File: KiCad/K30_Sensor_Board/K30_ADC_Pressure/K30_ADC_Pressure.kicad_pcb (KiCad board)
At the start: 2 copper layers, 100 x 50.8 mm, 156 parts, among them J1 CONN_02X12, J2 CONN_01X03, J3 CONN_01X05, J4 CONN_01X03, U1 ADS1015_VSSOP, U2 LPS25HB_HLGA

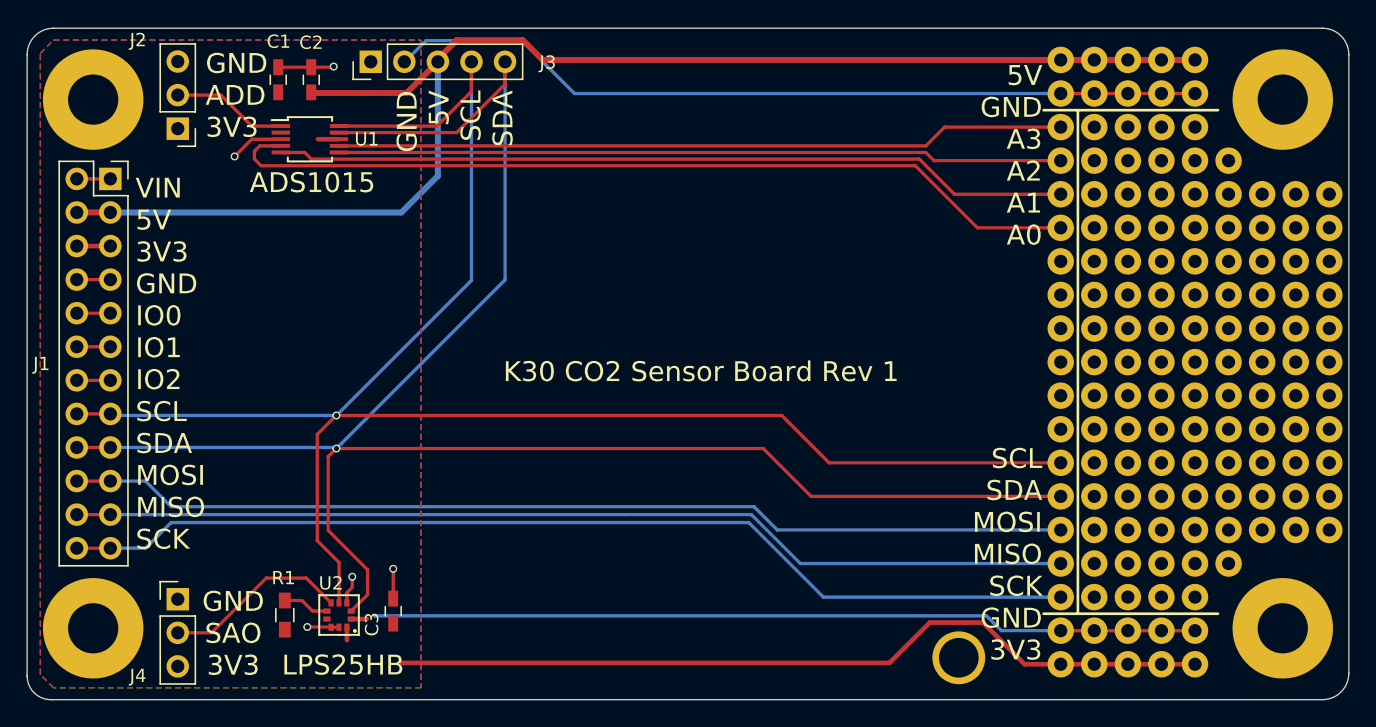
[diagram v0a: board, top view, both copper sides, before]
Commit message: minor changes to mounting hole
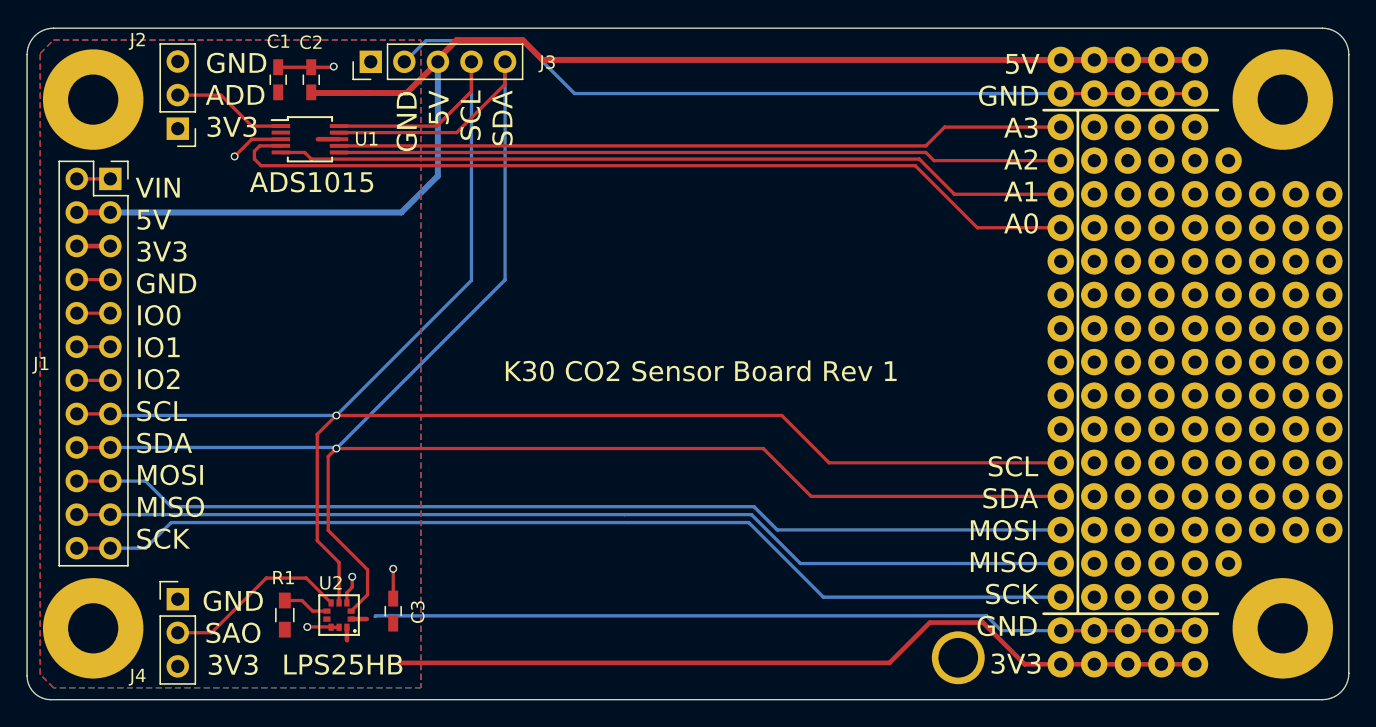
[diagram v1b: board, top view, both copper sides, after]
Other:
- rule trace_min: 0.2 -> 0.152
- board text added: "3V3"
- board text added: "5V GND A3 A2 A1 A0"
- board text added: "SCL SDA MOSI MISO SCK GND"
- board text removed: "5V GND A3 A2 A1 A0 SCL SDA MOSI MISO SCK GND 3V3"
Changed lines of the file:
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@@
     (area 90.745714 72.766666 204.069287 127.51)
     (thickness 1.6)
-    (drawings 20)
+    (drawings 22)
     (tracks 160)
     (zones 0)
@@
     (zone_clearance 0.508)
     (zone_45_only no)
-    (trace_min 0.2)
+    (trace_min 0.152)
     (segment_width 0.2)
     (edge_width 0.1)
@@
     (visible_elements 7FFCFFFF)
     (pcbplotparams
-      (layerselection 0x00030_80000001)
+      (layerselection 0x010f0_80000001)
       (usegerberextensions false)
       (excludeedgelayer true)
@@
       (outputformat 1)
       (mirror false)
-      (drillshape 1)
+      (drillshape 0)
       (scaleselection 1)
       (outputdirectory ""))
@@
   )
   (module Wire_Pads:SolderWirePad_single_1mmDrill (layer F.Cu)
-    (at 166.09 122.83)
+    (at 166.05 122.83)
     (fp_text reference REF** (at 0 -3.81) (layer F.SilkS) hide
       (effects (font (size 1 1) (thickness 0.15)))
@@
     (tags "capacitor 0603")
     (attr smd)
-    (fp_text reference C3 (at -1 -1.6 270) (layer F.SilkS)
+    (fp_text reference C3 (at -0.06 1.89 90) (layer F.SilkS)
       (effects (font (size 1 1) (thickness 0.15)))
     )
@@
       (net 2 /5V))
   )
+  (gr_text 3V3 (at 170.43 123.33) (layer F.SilkS)
+    (effects (font (size 1.5 1.5) (thickness 0.3)))
+  )
+  (gr_text "SCL\nSDA\nMOSI\nMISO\nSCK\nGND" (at 172.11 114.44) (layer F.SilkS)
+    (effects (font (size 1.5 1.5) (thickness 0.3)) (justify right))
+  )
   (gr_line (start 166.09 122.82) (end 166.09 122.83) (angle 90) (layer Eco1.User) (width 0.2))
   (gr_text "GND\nADD\n3V3" (at 109.1 80.3) (layer F.SilkS)
@@
     (effects (font (size 1.5 1.5) (thickness 0.3)))
   )
-  (gr_text "5V\nGND\nA3\nA2\nA1\nA0\n\n\n\n\n\n\nSCL\nSDA\nMOSI\nMISO\nSCK\nGND\n3V3" (at 172.42 100.53) (layer F.SilkS)
+  (gr_text "5V\nGND\nA3\nA2\nA1\nA0" (at 172.22 83.99) (layer F.SilkS)
     (effects (font (size 1.5 1.5) (thickness 0.3)) (justify right))
   )
@@
   (segment (start 133.1 76.1) (end 134.6 77.6) (width 0.45) (layer F.Cu) (net 2))
   (segment (start 128.1 76.1) (end 133.1 76.1) (width 0.45) (layer F.Cu) (net 2))
-  (segment (start 124.14 77.74) (end 124.18 77.74) (width 0.25) (layer B.Cu) (net 3) (status C00000))
-  (segment (start 124.18 77.74) (end 125.78 76.14) (width 0.25) (layer B.Cu) (net 3) (status 400000))
-  (segment (start 137.02 80.14) (end 173.8 80.14) (width 0.25) (layer B.Cu) (net 3) (status 800000))
+  (segment (start 124.14 77.74) (end 124.18 77.74) (width 0.25) (layer B.Cu) (net 3))
+  (segment (start 124.18 77.74) (end 125.78 76.14) (width 0.25) (layer B.Cu) (net 3))
+  (segment (start 137.02 80.14) (end 173.8 80.14) (width 0.25) (layer B.Cu) (net 3))
   (segment (start 133.02 76.14) (end 137.02 80.14) (width 0.25) (layer B.Cu) (net 3))
   (segment (start 125.78 76.14) (end 133.02 76.14) (width 0.25) (layer B.Cu) (net 3))
@@
   (segment (start 99.36 101.84) (end 101.9 101.84) (width 0.25) (layer F.Cu) (net 7))
   (segment (start 119 107) (end 118.98 107) (width 0.25) (layer F.Cu) (net 8))
-  (segment (start 121.36 118.06) (end 120.12 119.3) (width 0.25) (layer F.Cu) (net 8) (status 800000))
+  (segment (start 121.36 118.06) (end 120.12 119.3) (width 0.25) (layer F.Cu) (net 8))
   (segment (start 121.36 116.17) (end 121.36 118.06) (width 0.25) (layer F.Cu) (net 8))
   (segment (start 118.38 113.19) (end 121.36 116.17) (width 0.25) (layer F.Cu) (net 8))
@@
   (segment (start 101.9 106.92) (end 101.9 106.9) (width 0.25) (layer B.Cu) (net 8))
   (segment (start 119 104.5) (end 118.98 104.5) (width 0.25) (layer F.Cu) (net 9))
-  (segment (start 119.2 115.62) (end 119.2 118.68) (width 0.25) (layer F.Cu) (net 9) (status 800000))
+  (segment (start 119.2 115.62) (end 119.2 118.68) (width 0.25) (layer F.Cu) (net 9))
   (segment (start 117.55 113.97) (end 119.2 115.62) (width 0.25) (layer F.Cu) (net 9))
   (segment (start 117.55 105.93) (end 117.55 113.97) (width 0.25) (layer F.Cu) (net 9))

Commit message: added other kicad projects, sketchup solar model
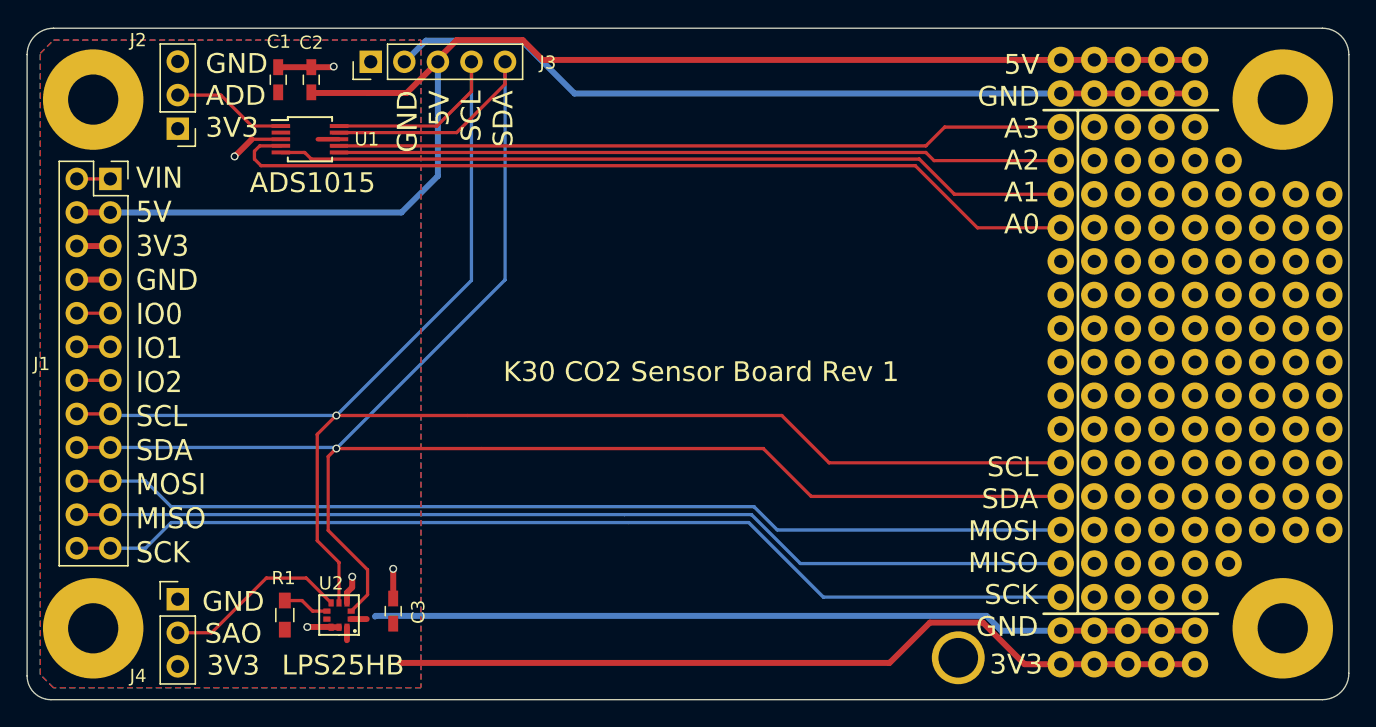
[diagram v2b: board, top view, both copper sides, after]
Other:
- net class 3V3: trace_width 0.35 -> 0.45
- net class GND added: clearance 0.14, trace_width 0.45, via_dia 0.6, via_drill 0.4
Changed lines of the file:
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@@
     (add_net /SDA)
     (add_net /VIN)
-    (add_net GND)
     (add_net "Net-(J2-Pad2)")
     (add_net "Net-(J3-Pad1)")
@@
   (net_class 3V3 ""
     (clearance 0.14)
-    (trace_width 0.35)
+    (trace_width 0.45)
     (via_dia 0.6)
     (via_drill 0.4)
@@
     (uvia_drill 0.1)
     (add_net /5V)
+  )
+  (net_class GND ""
+    (clearance 0.14)
+    (trace_width 0.45)
+    (via_dia 0.6)
+    (via_drill 0.4)
+    (uvia_dia 0.3)
+    (uvia_drill 0.1)
+    (add_net GND)
   )
   (module Wire_Pads:SolderWirePad_single_1mmDrill (layer F.Cu)
@@
     (effects (font (size 1.5 1.5) (thickness 0.3)))
   )
-  (gr_text "VIN\n5V\n3V3\nGND\nIO0\nIO1\nIO2\nSCL\nSDA\nMOSI\nMISO\nSCK" (at 103.8 100.6) (layer F.SilkS)
-    (effects (font (size 1.5 1.5) (thickness 0.3)) (justify left))
-  )
-  (segment (start 173.8 123.32) (end 171.07 123.32) (width 0.35) (layer F.Cu) (net 1))
-  (segment (start 123.87 123.22) (end 123.83 123.18) (width 0.35) (layer F.Cu) (net 1))
-  (segment (start 160.85 123.22) (end 123.87 123.22) (width 0.35) (layer F.Cu) (net 1))
-  (segment (start 163.9 120.17) (end 160.85 123.22) (width 0.35) (layer F.Cu) (net 1))
-  (segment (start 167.92 120.17) (end 163.9 120.17) (width 0.35) (layer F.Cu) (net 1))
-  (segment (start 171.07 123.32) (end 167.92 120.17) (width 0.35) (layer F.Cu) (net 1))
+  (gr_text "VIN\n5V\n3V3\nGND\nIO0\nIO1\nIO2\nSCL\nSDA\nMOSI\nMISO\nSCK" (at 103.83 100.7) (layer F.SilkS)
+    (effects (font (size 1.6 1.5) (thickness 0.3)) (justify left))
+  )
+  (segment (start 173.8 123.32) (end 171.07 123.32) (width 0.45) (layer F.Cu) (net 1))
+  (segment (start 123.87 123.22) (end 123.83 123.18) (width 0.45) (layer F.Cu) (net 1))
+  (segment (start 160.85 123.22) (end 123.87 123.22) (width 0.45) (layer F.Cu) (net 1))
+  (segment (start 163.9 120.17) (end 160.85 123.22) (width 0.45) (layer F.Cu) (net 1))
+  (segment (start 167.92 120.17) (end 163.9 120.17) (width 0.45) (layer F.Cu) (net 1))
+  (segment (start 171.07 123.32) (end 167.92 120.17) (width 0.45) (layer F.Cu) (net 1))
   (segment (start 119.2 83.6) (end 117.6 83.6) (width 0.35) (layer F.Cu) (net 1))
-  (segment (start 119.8 120.52) (end 119.8 121.5) (width 0.35) (layer F.Cu) (net 1))
-  (segment (start 120.12 119.9) (end 121.3 119.9) (width 0.35) (layer F.Cu) (net 1))
-  (segment (start 183.96 123.32) (end 181.42 123.32) (width 0.35) (layer F.Cu) (net 1))
-  (segment (start 181.42 123.32) (end 178.88 123.32) (width 0.35) (layer F.Cu) (net 1))
-  (segment (start 178.88 123.32) (end 176.34 123.32) (width 0.35) (layer F.Cu) (net 1))
-  (segment (start 176.34 123.32) (end 173.8 123.32) (width 0.35) (layer F.Cu) (net 1))
-  (segment (start 99.36 91.68) (end 101.9 91.68) (width 0.35) (layer F.Cu) (net 1))
+  (segment (start 119.8 120.52) (end 119.8 121.5) (width 0.45) (layer F.Cu) (net 1))
+  (segment (start 120.12 119.9) (end 121.3 119.9) (width 0.45) (layer F.Cu) (net 1))
+  (segment (start 183.96 123.32) (end 181.42 123.32) (width 0.45) (layer F.Cu) (net 1))
+  (segment (start 181.42 123.32) (end 178.88 123.32) (width 0.45) (layer F.Cu) (net 1))
+  (segment (start 178.88 123.32) (end 176.34 123.32) (width 0.45) (layer F.Cu) (net 1))
+  (segment (start 176.34 123.32) (end 173.8 123.32) (width 0.45) (layer F.Cu) (net 1))
+  (segment (start 99.36 91.68) (end 101.9 91.68) (width 0.45) (layer F.Cu) (net 1))
   (segment (start 126.68 77.74) (end 126.68 86.38) (width 0.45) (layer B.Cu) (net 2))
   (segment (start 123.92 89.14) (end 101.9 89.14) (width 0.45) (layer B.Cu) (net 2))
@@
   (segment (start 133.1 76.1) (end 134.6 77.6) (width 0.45) (layer F.Cu) (net 2))
   (segment (start 128.1 76.1) (end 133.1 76.1) (width 0.45) (layer F.Cu) (net 2))
-  (segment (start 124.14 77.74) (end 124.18 77.74) (width 0.25) (layer B.Cu) (net 3))
-  (segment (start 124.18 77.74) (end 125.78 76.14) (width 0.25) (layer B.Cu) (net 3))
-  (segment (start 137.02 80.14) (end 173.8 80.14) (width 0.25) (layer B.Cu) (net 3))
-  (segment (start 133.02 76.14) (end 137.02 80.14) (width 0.25) (layer B.Cu) (net 3))
-  (segment (start 125.78 76.14) (end 133.02 76.14) (width 0.25) (layer B.Cu) (net 3))
-  (segment (start 173.8 120.78) (end 169.31 120.78) (width 0.25) (layer B.Cu) (net 3))
-  (segment (start 121.97 119.66) (end 121.92 119.71) (width 0.25) (layer B.Cu) (net 3))
-  (segment (start 168.19 119.66) (end 121.97 119.66) (width 0.25) (layer B.Cu) (net 3))
-  (segment (start 169.31 120.78) (end 168.19 119.66) (width 0.25) (layer B.Cu) (net 3))
+  (segment (start 124.14 77.74) (end 124.18 77.74) (width 0.45) (layer B.Cu) (net 3))
+  (segment (start 124.18 77.74) (end 125.78 76.14) (width 0.45) (layer B.Cu) (net 3))
+  (segment (start 137.02 80.14) (end 173.8 80.14) (width 0.45) (layer B.Cu) (net 3))
+  (segment (start 133.02 76.14) (end 137.02 80.14) (width 0.45) (layer B.Cu) (net 3))
+  (segment (start 125.78 76.14) (end 133.02 76.14) (width 0.45) (layer B.Cu) (net 3))
+  (segment (start 173.8 120.78) (end 169.31 120.78) (width 0.45) (layer B.Cu) (net 3))
+  (segment (start 121.97 119.66) (end 121.92 119.71) (width 0.45) (layer B.Cu) (net 3))
+  (segment (start 168.19 119.66) (end 121.97 119.66) (width 0.45) (layer B.Cu) (net 3))
+  (segment (start 169.31 120.78) (end 168.19 119.66) (width 0.45) (layer B.Cu) (net 3))
   (segment (start 114.8 83.6) (end 112.6 83.6) (width 0.25) (layer F.Cu) (net 3))
   (via (at 111.3 84.9) (size 0.6) (drill 0.4) (layers F.Cu B.Cu) (net 3))
-  (segment (start 112.6 83.6) (end 111.3 84.9) (width 0.25) (layer F.Cu) (net 3))
-  (segment (start 114.6 78.15) (end 117.1 78.15) (width 0.25) (layer F.Cu) (net 3))
-  (segment (start 119.8 118.68) (end 119.8 117.9) (width 0.25) (layer F.Cu) (net 3))
+  (segment (start 112.6 83.6) (end 111.3 84.9) (width 0.45) (layer F.Cu) (net 3))
+  (segment (start 114.6 78.15) (end 117.1 78.15) (width 0.45) (layer F.Cu) (net 3))
+  (segment (start 119.8 118.68) (end 119.8 117.9) (width 0.45) (layer F.Cu) (net 3))
   (via (at 120.2 116.7) (size 0.6) (drill 0.4) (layers F.Cu B.Cu) (net 3))
-  (segment (start 120.2 117.5) (end 120.2 116.7) (width 0.25) (layer F.Cu) (net 3))
-  (segment (start 119.8 117.9) (end 120.2 117.5) (width 0.25) (layer F.Cu) (net 3))
-  (segment (start 123.3 118.35) (end 123.3 116.1) (width 0.25) (layer F.Cu) (net 3))
+  (segment (start 120.2 117.5) (end 120.2 116.7) (width 0.45) (layer F.Cu) (net 3))
+  (segment (start 119.8 117.9) (end 120.2 117.5) (width 0.45) (layer F.Cu) (net 3))
+  (segment (start 123.3 118.35) (end 123.3 116.1) (width 0.45) (layer F.Cu) (net 3))
   (via (at 123.3 116.1) (size 0.6) (drill 0.4) (layers F.Cu B.Cu) (net 3))
-  (segment (start 119.2 120.52) (end 118.6 120.52) (width 0.25) (layer F.Cu) (net 3))
-  (segment (start 118.6 120.52) (end 118.58 120.5) (width 0.25) (layer F.Cu) (net 3))
-  (segment (start 118.58 120.5) (end 116.8 120.5) (width 0.25) (layer F.Cu) (net 3))
+  (segment (start 119.2 120.52) (end 118.6 120.52) (width 0.45) (layer F.Cu) (net 3))
+  (segment (start 118.6 120.52) (end 118.58 120.5) (width 0.45) (layer F.Cu) (net 3))
+  (segment (start 118.58 120.5) (end 116.8 120.5) (width 0.45) (layer F.Cu) (net 3))
   (via (at 116.8 120.5) (size 0.6) (drill 0.4) (layers F.Cu B.Cu) (net 3))
-  (segment (start 173.8 120.78) (end 176.34 120.78) (width 0.25) (layer F.Cu) (net 3))
-  (segment (start 176.34 120.78) (end 178.88 120.78) (width 0.25) (layer F.Cu) (net 3))
-  (segment (start 178.88 120.78) (end 181.42 120.78) (width 0.25) (layer F.Cu) (net 3))
-  (segment (start 181.42 120.78) (end 183.96 120.78) (width 0.25) (layer F.Cu) (net 3))
-  (segment (start 173.8 80.14) (end 176.34 80.14) (width 0.25) (layer F.Cu) (net 3))
-  (segment (start 176.34 80.14) (end 178.88 80.14) (width 0.25) (layer F.Cu) (net 3))
-  (segment (start 178.88 80.14) (end 181.42 80.14) (width 0.25) (layer F.Cu) (net 3))
-  (segment (start 181.42 80.14) (end 183.96 80.14) (width 0.25) (layer F.Cu) (net 3))
-  (segment (start 99.36 94.22) (end 101.9 94.22) (width 0.25) (layer F.Cu) (net 3))
-  (segment (start 117.1 78.15) (end 118.75 78.15) (width 0.25) (layer F.Cu) (net 3))
+  (segment (start 173.8 120.78) (end 176.34 120.78) (width 0.45) (layer F.Cu) (net 3))
+  (segment (start 176.34 120.78) (end 178.88 120.78) (width 0.45) (layer F.Cu) (net 3))
+  (segment (start 178.88 120.78) (end 181.42 120.78) (width 0.45) (layer F.Cu) (net 3))
+  (segment (start 181.42 120.78) (end 183.96 120.78) (width 0.45) (layer F.Cu) (net 3))
+  (segment (start 173.8 80.14) (end 176.34 80.14) (width 0.45) (layer F.Cu) (net 3))
+  (segment (start 176.34 80.14) (end 178.88 80.14) (width 0.45) (layer F.Cu) (net 3))
+  (segment (start 178.88 80.14) (end 181.42 80.14) (width 0.45) (layer F.Cu) (net 3))
+  (segment (start 181.42 80.14) (end 183.96 80.14) (width 0.45) (layer F.Cu) (net 3))
+  (segment (start 99.36 94.22) (end 101.9 94.22) (width 0.45) (layer F.Cu) (net 3))
+  (segment (start 117.1 78.15) (end 118.75 78.15) (width 0.45) (layer F.Cu) (net 3))
   (via (at 118.8 78.1) (size 0.6) (drill 0.4) (layers F.Cu B.Cu) (net 3))
-  (segment (start 118.75 78.15) (end 118.8 78.1) (width 0.25) (layer F.Cu) (net 3))
-  (segment (start 124.14 77.74) (end 124.14 77.26) (width 0.25) (layer B.Cu) (net 3))
-  (segment (start 124.1 77.78) (end 124.14 77.74) (width 0.25) (layer F.Cu) (net 3))
-  (segment (start 124.1 77.78) (end 124.14 77.74) (width 0.25) (layer F.Cu) (net 3))
+  (segment (start 118.75 78.15) (end 118.8 78.1) (width 0.45) (layer F.Cu) (net 3))
+  (segment (start 124.14 77.74) (end 124.14 77.26) (width 0.45) (layer B.Cu) (net 3))
+  (segment (start 124.1 77.78) (end 124.14 77.74) (width 0.45) (layer F.Cu) (net 3))
+  (segment (start 124.1 77.78) (end 124.14 77.74) (width 0.45) (layer F.Cu) (net 3))
   (segment (start 99.36 86.6) (end 101.9 86.6) (width 0.25) (layer F.Cu) (net 4))
   (segment (start 99.36 96.76) (end 101.9 96.76) (width 0.25) (layer F.Cu) (net 5))
